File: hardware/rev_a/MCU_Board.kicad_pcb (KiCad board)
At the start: 2 copper layers, 30 x 55 mm, 28 parts, among them J1 ST-Link, J2 Conn_01x08, J3 Bus, J4 Conn_01x08, J5 Conn_02x07_Odd_Even, SW1 nRST, U1 STM32F042K6Tx, U3 SN65HVD230, U4 LP2985-3.3, Y1 8Mhz

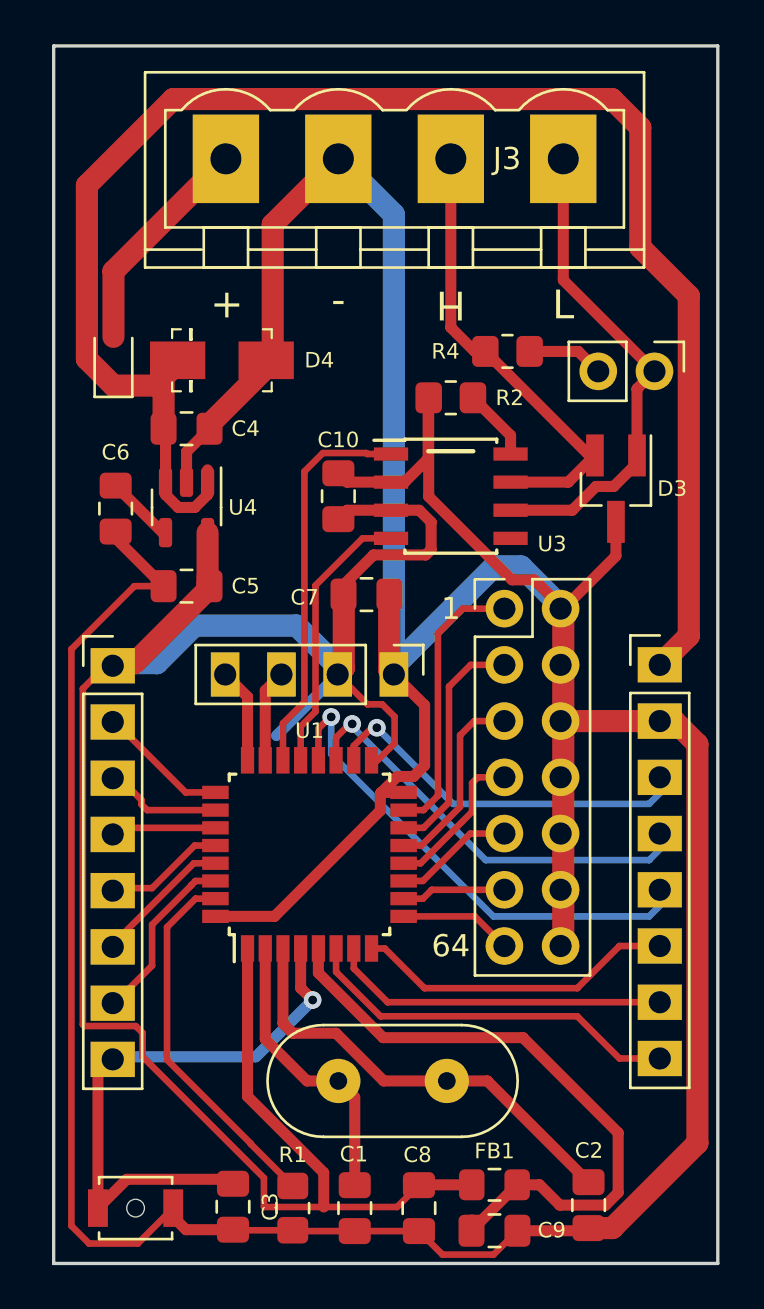
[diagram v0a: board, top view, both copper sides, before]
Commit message: Fix all the warnings or errors and add the 'fab' folder with all the required files for production.
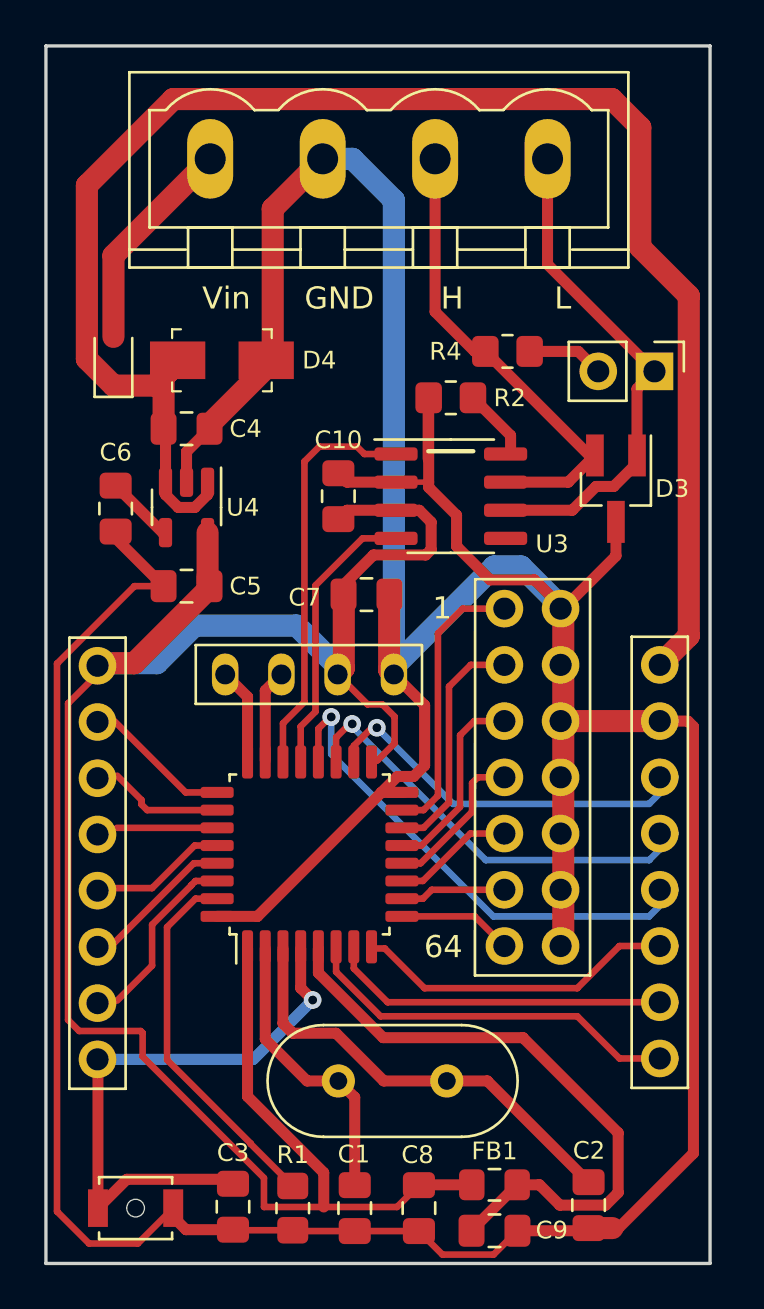
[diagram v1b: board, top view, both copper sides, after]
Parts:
- D4: footprint digikey-footprints:DO-214AC -> custom:DO-214AA
- J1: footprint Connector_PinHeader_2.54mm:PinHeader_1x04_P2.54mm_Vertical -> custom:st-link
- J2, J4: footprint Connector_PinHeader_2.54mm:PinHeader_1x08_P2.54mm_Vertical -> custom:CONN_01x08
- J3: footprint Connector_Phoenix_MSTB:PhoenixContact_MSTBVA_2,5_4-G-5,08_1x04_P5.08mm_Vertical -> custom:PhoenixContact_MSTBVA_2,5_4-G-5,08_1x04_P5.08mm_Vertical_custom
- J5: footprint Connector_PinHeader_2.54mm:PinHeader_2x07_P2.54mm_Vertical -> custom:addr_jumpers
- moved J3 0.71 mm to (88.9, 104.1)
- moved J2 0.69 mm to (68.6, 127.0)
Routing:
- net /VDD: track 97.9 -> 93.3 mm
- net /nRST: track 26.8 -> 25.3 mm
- net /PA10: track 23.9 -> 23.0 mm
- net /VIN: track 75.7 -> 75.0 mm
- net /ADDR_32: track 5.28 -> 4.72 mm
- net /CAN_TX: track 17.7 -> 18.2 mm
- net /VDDA: track 28.9 -> 28.4 mm
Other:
- board text added: "GND"
- board text added: "Vin"
- board text removed: "+"
- board text removed: "-"
